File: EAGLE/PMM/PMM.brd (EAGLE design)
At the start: 76.2 x 50.8 mm, 23 parts, among them J1 TB001-500-12BE, K1 EC2-5NU, K2 G6DN-1A_DC5, K3 35701331, K4 35701331

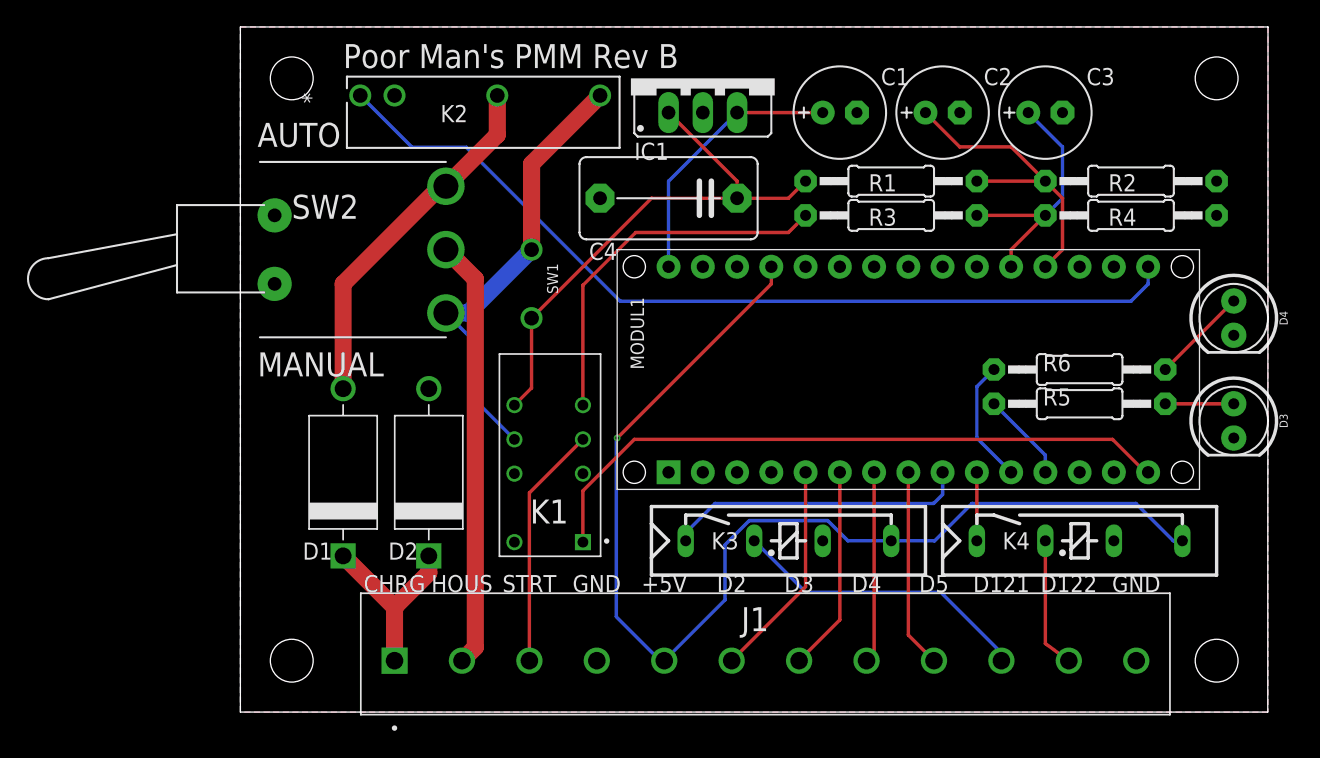
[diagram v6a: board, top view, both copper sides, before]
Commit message: Changed spare DIO to 2 in, 2 out, all relay isolated
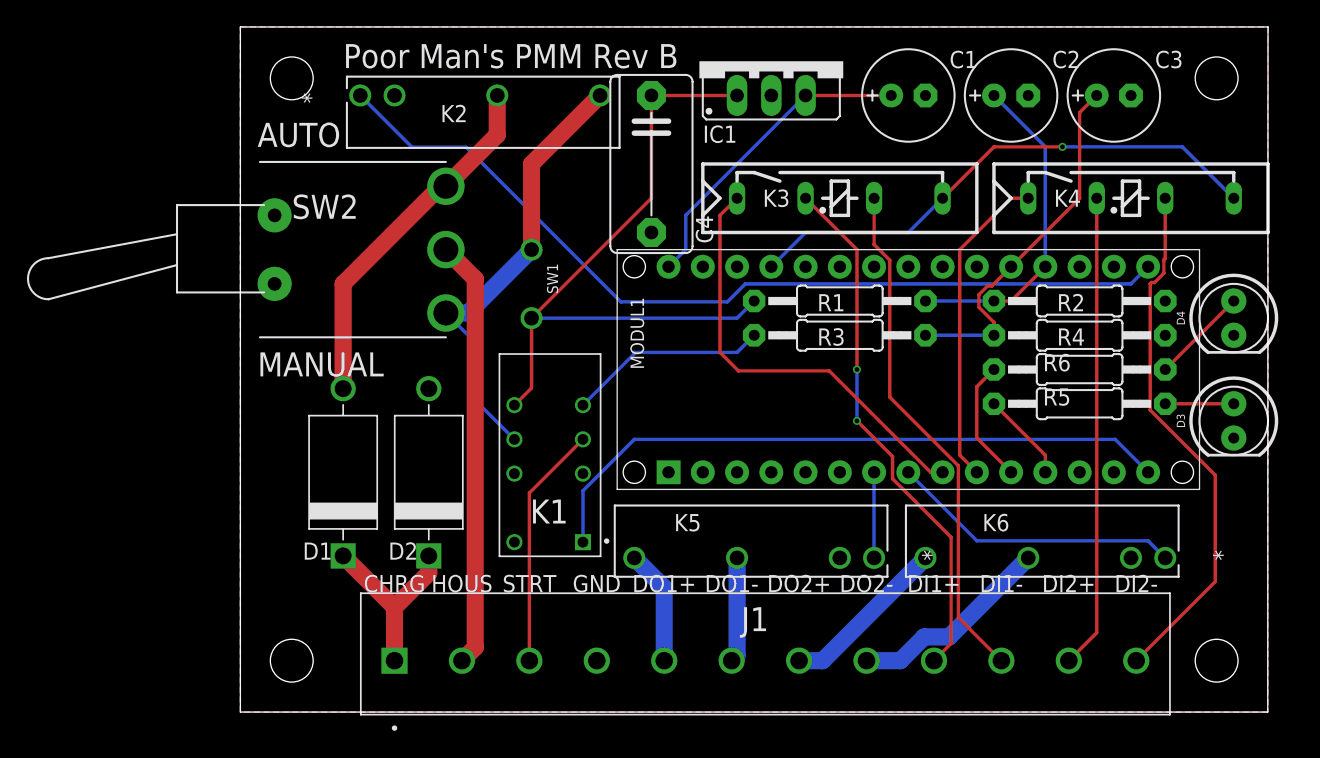
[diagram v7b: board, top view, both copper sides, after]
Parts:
- added K5, K6: G6DN-1A_DC5, G6DN:RELAY_G6DN-1A_OMR
- moved K3 25.7 mm to (54.6, 35.6)
- moved K4 25.7 mm to (76.2, 35.6)
- moved R2 9.67 mm to (62.2, 30.5)
- moved R4 9.67 mm to (62.2, 27.9)
- moved R1 9.67 mm to (44.5, 30.5)
- moved R3 9.67 mm to (44.5, 27.9)
- moved C1 5.24 mm to (49.5, 45.7)
- moved C2 5.24 mm to (57.1, 45.7)
- moved C3 5.24 mm to (64.8, 45.7)
- moved IC1 5.24 mm to (39.4, 48.3)
- moved C4 2.84 mm to (30.5, 40.6), turned to 270 degrees
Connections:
- new net N$26: J1.5, K5.8
- new net N$27: J1.6, K5.5
- new net N$28: J1.7, K6.8
- new net N$29: J1.8, K6.5
- net GND: now also K5.2, K6.2; no longer J1.12, K3.5, K4.5
- net N$13: no longer J1.5
- net N$14: now also J1.9, K3.3; no longer J1.6, MODUL1.J1.5
- net N$15: now also J1.12, K4.5; no longer J1.7, MODUL1.J1.6
- net N$16: now also J1.10, K3.5; no longer J1.8, MODUL1.J1.7
- net N$17: now also K6.1; no longer J1.9
- net N$18: now also K5.1, MODUL1.J1.7; no longer J1.10, K3.3
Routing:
- net N$13: track 83.6 -> 39.6 mm
- net N$20: track 9.77 -> 35.1 mm
- net N$15: track 15.2 -> 39.3 mm
- net N$16: track 14.5 -> 38.2 mm
- net N$14: track 16.2 -> 39.3 mm, vias 0 -> 2
- net N$21: track 5.08 -> 23.7 mm
- net N$18: track 22.4 -> 6.35 mm
- net N$29: track 0.00 -> 15.1 mm
- net N$12: track 27.5 -> 14.9 mm
- net N$28: track 0.00 -> 12.5 mm
- net N$4: track 40.0 -> 50.6 mm
- net N$19: track 22.5 -> 32.1 mm
- net N$26: track 0.00 -> 8.54 mm
- net N$11: track 19.1 -> 27.1 mm
- net N$27: track 0.00 -> 7.79 mm
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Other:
- board text added: "DI1+"
- board text added: "DI1-"
- board text added: "DI2+"
- board text added: "DI2-"
- board text added: "DO1+"
- board text added: "DO1-"
- board text added: "DO2+"
- board text added: "DO2-"
- board text removed: "+5V"
- board text removed: "D121"
- board text removed: "D122"
- board text removed: "D2"
- board text removed: "D3"
- board text removed: "D4"
- board text removed: "D5"
